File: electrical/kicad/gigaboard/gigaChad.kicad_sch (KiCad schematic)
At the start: 58 parts, among them J1 Conn_01x04, J10 Conn_01x04, J11 Conn_01x06, J2 Conn_02x03_Top_Bottom, J3 Conn_01x04, J4 Conn_02x03_Top_Bottom, J5 Conn_02x03_Top_Bottom, J6 Conn_01x04, J7 Conn_02x03_Top_Bottom, J8 Conn_01x04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

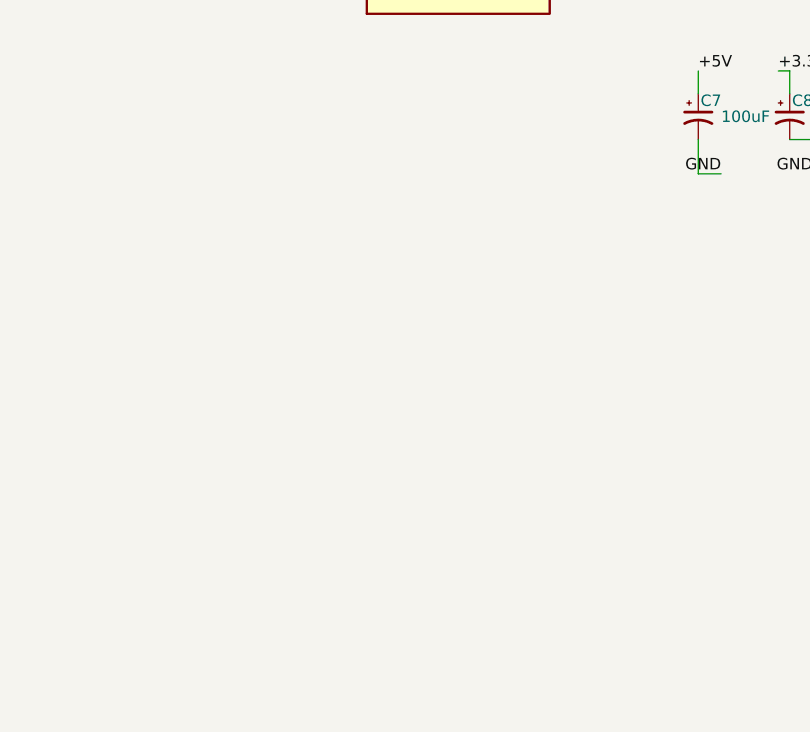
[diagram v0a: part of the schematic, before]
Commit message: modify(giga): add sensors, motor drivers
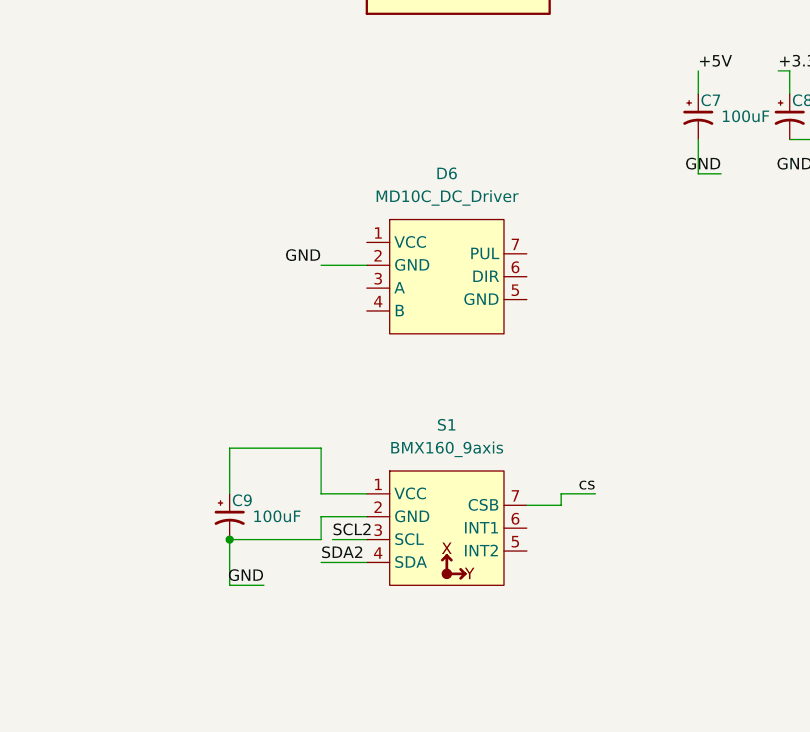
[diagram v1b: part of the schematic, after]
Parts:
- added C9: 100uF, Capacitor_THT:C_Radial_D4.0mm_H5.0mm_P1.50mm, symbol ControlPCB-rescue:CP1_Small
- added D6: MD10C_DC_Driver, symbol Motor_Driver:MD10C_DC_Driver
- added S1: BMX160_9axis, symbol Sensors:BMX160_9axis
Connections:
- net GND: now also C9.2, D6.2 (GND), S1.2 (GND)
- net SCL2: now also S1.3 (SCL)
- net SDA2: now also S1.4 (SDA)
- new net: C9.1, S1.1 (VCC)
- new net cs: S1.7 (CSB)
